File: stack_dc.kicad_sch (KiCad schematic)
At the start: 1 part, among them Q1 IRFZ44NPBF

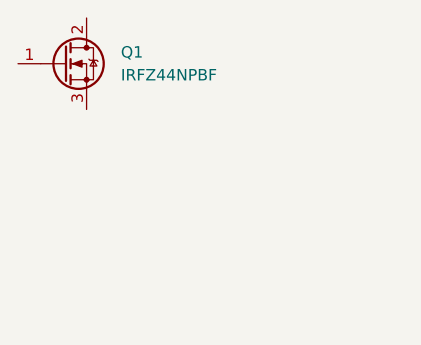
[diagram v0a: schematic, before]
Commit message: start place component
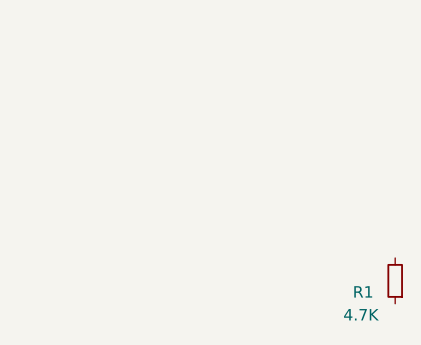
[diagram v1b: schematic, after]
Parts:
- removed Q1: IRFZ44NPBF, Package_TO_SOT_THT:TO-220-3_Vertical, symbol New_Library:IRFZ44N
- added R1: 4.7K, Resistor_SMD:R_1206_3216Metric_Pad1.30x1.75mm_HandSolder, symbol Device:R_Small
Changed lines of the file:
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@@
-(kicad_sch (version 20230121) (generator eeschema)
-  (paper "A3")
-  (symbol (lib_id "New_Library:IRFZ44N") (at 163.83 91.44 0) (unit 1)
-    (in_bom yes) (on_board yes) (dnp no) (fields_autoplaced)
-    (property "Reference" "Q1" (at 170.18 90.17 0)
-      (effects (font (size 1.27 1.27)) (justify left))
-    )
-    (property "Value" "IRFZ44NPBF" (at 170.18 92.71 0)
-      (effects (font (size 1.27 1.27)) (justify left))
-    )
-    (property "Footprint" "Package_TO_SOT_THT:TO-220-3_Vertical" (at 170.18 93.345 0)
-      (effects (font (size 1.27 1.27) italic) (justify left) hide)
-    )
-    (property "Datasheet" "https://www.mouser.kr/datasheet/2/196/Infineon_IRFZ44N_DataSheet_v01_01_EN-3166504.pdf" (at 163.83 91.44 0)
-      (effects (font (size 1.27 1.27)) (justify left) hide)
-    )
-    (pin "1")
-    (pin "2")
-    (pin "3")
-    (instances
-      (project "24V_Inv"
-        (path "/3c92cd3e-3830-47e7-9963-31800eeabf85/03848658-1525-4110-bf96-0f22b071072d"
-          (reference "Q1") (unit 1)
-        )
-      )
-    )
-  )
+(kicad_sch
+	(version 20231120)
+	(generator "eeschema")
+	(generator_version "8.0")
+	(paper "A3")
+	(symbol
+		(lib_id "Device:R_Small")
+		(at 200.66 115.57 180)
+		(unit 1)
+		(exclude_from_sim no)
+		(in_bom yes)
+		(on_board yes)
+		(dnp no)
+		(property "Reference" "R1"
+			(at 197.104 116.84 0)
+			(effects
+				(font
+					(size 1.27 1.27)
+				)
+			)
+		)
+		(property "Value" "4.7K"
+			(at 196.85 119.38 0)
+			(effects
+				(font
+					(size 1.27 1.27)
+				)
+			)
+		)
+		(property "Footprint" "Resistor_SMD:R_1206_3216Metric_Pad1.30x1.75mm_HandSolder"
+			(at 200.66 115.57 0)
+			(effects
+				(font
+					(size 1.27 1.27)
+				)
+				(hide yes)
+			)
+		)
+		(property "Datasheet" "https://www.vishay.com/docs/20066/rcce3.pdf"
+			(at 200.66 115.57 0)
+			(effects
+				(font
+					(size 1.27 1.27)
+				)
+				(hide yes)
+			)
+		)
+		(property "Description" "Thick Film Resistors 4.7 Kohms 1% 100ppm"
+			(at 200.66 115.57 0)
+			(effects
+				(font
+					(size 1.27 1.27)
+				)
+				(hide yes)
+			)
+		)
+		(property "Height" "0.95"
+			(at 200.66 115.57 90)
+			(effects
+				(font
+					(size 1.27 1.27)
+				)
+				(hide yes)
+			)
+		)
+		(property "Mouser Part Number" "71-RCC12064K70FKEA"
+			(at 200.66 115.57 90)
+			(effects
+				(font
+					(size 1.27 1.27)
+				)
+				(hide yes)
+			)
+		)
+		(property "Mouser Price/Stock" "https://www.mouser.kr/ProductDetail/Vishay-Dale/RCC12064K70FKEA?qs=sGAEpiMZZMvdGkrng054twKDKoBh%252BscnGARE0HO91459ssjkSfCCHA%3D%3D"
+			(at 200.66 115.57 90)
+			(effects
+				(font
+					(size 1.27 1.27)
+				)
+				(hide yes)
+			)
+		)
+		(property "Manufacturer_Name" "Vishay / Dale"
+			(at 200.66 115.57 90)
+			(effects
+				(font
+					(size 1.27 1.27)
+				)
+				(hide yes)
+			)
+		)
+		(property "Manufacturer_Part_Number" "RCC12064K70FKEA"
+			(at 200.66 115.57 90)
+			(effects
+				(font
+					(size 1.27 1.27)
+				)
+				(hide yes)
+			)
+		)
+		(property "Cost" "350"
+			(at 200.66 115.57 90)
+			(effects
+				(font
+					(size 1.27 1.27)
+				)
+				(hide yes)
+			)
+		)
+		(pin "1"
+		)
+		(pin "2"
+		)
+		(instances
+			(project "stack_dc"
+				(path "/89ce1d2c-cc8a-423d-968d-c47340f04443"
+					(reference "R1")
+					(unit 1)
+				)
+			)
+		)
+	)
+	(sheet_instances
+		(path "/"
+			(page "1")
+		)
+	)
 )
